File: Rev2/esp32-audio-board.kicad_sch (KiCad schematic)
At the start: 129 parts, among them IC1 LP2985A-33DBVR, J2 JST S2B, J21 IO32_PAD0, J3 USB_C_Receptacle_USB2.0_16P, J5 IO32_PAD1, J6 IO33_PAD0, J7 IO33_PAD1, J8 IO25_PAD0, J9 IO25_PAD1, Q1 SS8050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

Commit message: esp32-audio-board: add initial Rev2 schematic
Added an initial Rev2 schematic that contains all the main
components, except the connector to the sense board. This
can be decided later.
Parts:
- removed C39: 22uF/10%, Capacitor_SMD:C_0402_1005Metric_Pad0.74x0.62mm_HandSolder, symbol Device:C
- removed H4: MountingHole_Pad, MountingHole:MountingHole_2.2mm_M2_Pad_TopOnly, symbol Mechanical:MountingHole_Pad
- removed HP_G2: HP_GND2, solderpads:SolderPad_SMD_2x3mm, symbol Connector:Conn_01x01_Pin
- removed HP_L2: HP_LOUT2, solderpads:SolderPad_SMD_2x3mm, symbol Connector:Conn_01x01_Pin
- removed HP_R2: HP_ROUT2, solderpads:SolderPad_SMD_2x3mm, symbol Connector:Conn_01x01_Pin
- removed J2: JST S2B, Connector_JST:JST_PH_S2B-PH-K_1x02_P2.00mm_Horizontal, symbol Connector:Conn_01x02_Pin
- removed R32: 33R/1%, Resistor_SMD:R_0402_1005Metric_Pad0.72x0.64mm_HandSolder, symbol Device:R_US
- removed R37, R38: 100K/1%, Resistor_SMD:R_0402_1005Metric_Pad0.72x0.64mm_HandSolder, symbol Device:R_US
- removed TP1: T_SCL, TestPoint:TestPoint_Pad_D1.0mm, symbol Connector:TestPoint_Probe
- removed TP2: T_SDA, TestPoint:TestPoint_Pad_D1.0mm, symbol Connector:TestPoint_Probe
- added IC2: MAX17048G+T10, SON50P200X200X80-9N-D, symbol MAX17048G+T10:MAX17048G+T10
- added J1, J2: Conn_01x01_Pin, solderpads:SolderPad_SMD_2x2mm, symbol Connector:Conn_01x01_Pin
- C38: value 22uF/10% -> 0.1uF/10%
- R31: value 33R/1% -> 2K
- U2: DESCRIPTION USB to UART Bridge -> (none)
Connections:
- net ESP_IO35 is gone; now on net !ALRT: U1.7 (IO35)
- net +3V3: now also R31.1
- net ESP-IO0: no longer R24.1
- net GND: now also C38.2, IC2.1 (CTG), IC2.4 (GND), IC2.6 (QSTRT), IC2.9 (EP), J2.1 (Pin_1)
- net SCL: now also R23.2, IC2.7 (SCL); no longer R22.2
- net SDA: now also R22.2, IC2.8 (SDA); no longer R23.2
- net Serial-TX: now also R24.1
- net VBAT: now also C38.1, IC2.2 (CELL), IC2.3 (VDD), J1.1 (Pin_1)
- net !ALRT: now reaches R31.2
- net !ALRT: now also IC2.5 (~{ALRT})
- net ES8388_LOUT2: no longer names the net of U5.15 (LOUT2)
- net ES8388_LOUT2: no longer C38.1
- net ES8388_ROUT2: no longer names the net of U5.14 (ROUT2)
- no-connect marks 25 -> 27
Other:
- note added: "Fuel Gauge"
- note added: "I2C pull-ups"
- note added: "Place near the ESP32 module"
- note removed: "Battery Monitor"
- moved on the sheet: C19, C20, C21, C22, C23, C24, C25, C26, C27, C28, C29, C30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

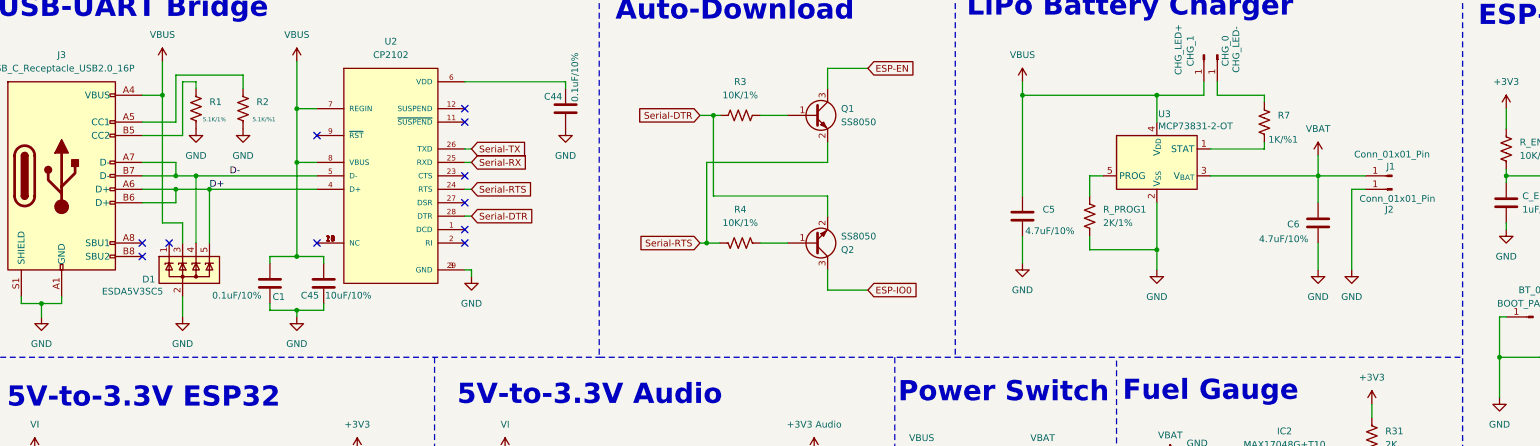
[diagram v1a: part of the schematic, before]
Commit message: esp32-audio-board: initial Rev2 PCB
Started working on the Rev2 PCB. Managed to get components
a lot closer and the PCB layout is more compact. The PCB
width got smaller by ~10mm.
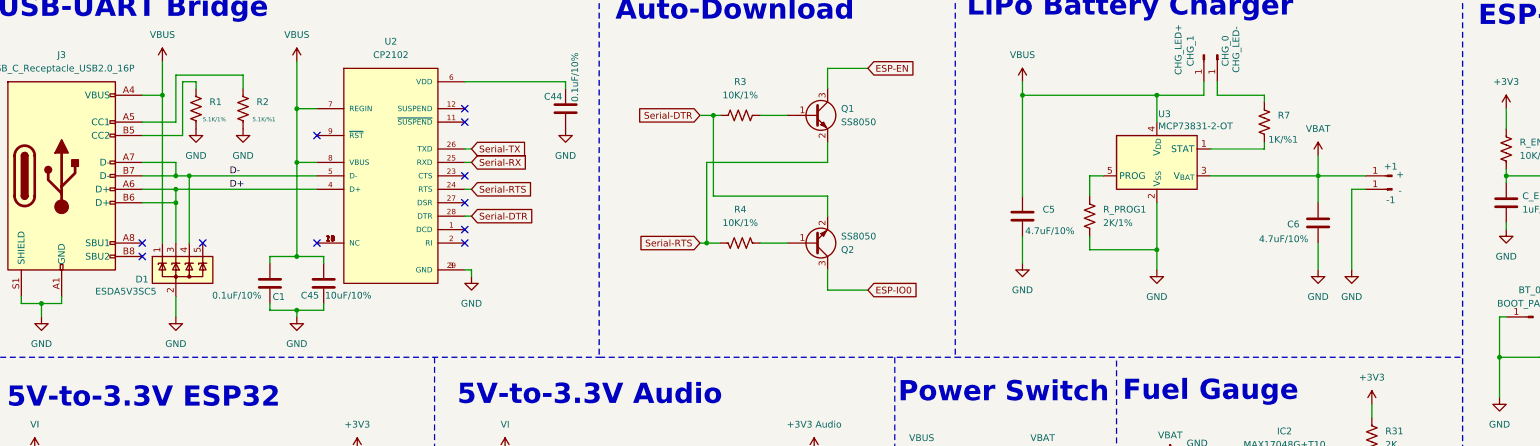
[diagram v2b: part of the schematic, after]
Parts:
- +1: renamed from J1; value Conn_01x01_Pin -> +
- -1: renamed from J2; value Conn_01x01_Pin -> -
- CHG_0, CHG_1, PWR_0, PWR_1: footprint solderpads:SolderPad_SMD_2x2mm -> solderpads:SolderPad_SMD_1x1mm
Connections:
- net D+: now also D1.3 (K); no longer D1.5 (K)
- net VBUS: now also D1.1 (K); no longer D1.3 (K)
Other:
- moved on the sheet: D1
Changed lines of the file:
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@@
 	)
 	(junction
-		(at 55.88 53.34)
+		(at 22.86 114.3)
 		(diameter 0)
 		(color 0 0 0 0)
 	)
 	(junction
-		(at 22.86 114.3)
+		(at 38.1 114.3)
 		(diameter 0)
 		(color 0 0 0 0)
 	)
 	(junction
-		(at 38.1 114.3)
+		(at 95.25 228.6)
 		(diameter 0)
 		(color 0 0 0 0)
 	)
 	(junction
-		(at 95.25 228.6)
+		(at 52.07 50.8)
 		(diameter 0)
 		(color 0 0 0 0)
@@
 	)
 	(junction
+		(at 49.53 55.88)
+		(diameter 0)
+		(color 0 0 0 0)
+	)
+	(junction
 		(at 24.13 74.93)
 		(diameter 0)
@@
 	)
 	(junction
-		(at 53.34 50.8)
-		(diameter 0)
-		(color 0 0 0 0)
-	)
-	(junction
 		(at 167.64 234.95)
 		(diameter 0)
@@
 	)
 	(no_connect
-		(at 48.26 63.5)
-	)
-	(no_connect
 		(at 370.84 91.44)
 	)
@@
 	)
 	(no_connect
+		(at 54.61 63.5)
+	)
+	(no_connect
 		(at 370.84 86.36)
 	)
@@
 	(wire
 		(pts
-			(xy 49.53 53.34) (xy 55.88 53.34)
+			(xy 49.53 53.34) (xy 76.2 53.34)
 		)
 		(stroke
@@
 	(wire
 		(pts
-			(xy 46.99 35.56) (xy 46.99 59.69)
+			(xy 46.99 35.56) (xy 46.99 63.5)
 		)
 		(stroke
@@
 	(wire
 		(pts
-			(xy 55.88 53.34) (xy 55.88 63.5)
-		)
-		(stroke
-			(width 0)
-			(type default)
-		)
-	)
-	(wire
-		(pts
 			(xy 368.3 189.23) (xy 368.3 193.04)
 		)
@@
 	(wire
 		(pts
-			(xy 50.8 73.66) (xy 50.8 77.47)
+			(xy 49.53 73.66) (xy 49.53 77.47)
 		)
 		(stroke
@@
 	(wire
 		(pts
-			(xy 53.34 50.8) (xy 76.2 50.8)
+			(xy 49.53 50.8) (xy 52.07 50.8)
 		)
 		(stroke
@@
 	(wire
 		(pts
-			(xy 50.8 59.69) (xy 50.8 63.5)
-		)
-		(stroke
-			(width 0)
-			(type default)
-		)
-	)
-	(wire
-		(pts
 			(xy 111.76 120.65) (xy 118.11 120.65)
 		)
@@
 	(wire
 		(pts
-			(xy 55.88 53.34) (xy 76.2 53.34)
-		)
-		(stroke
-			(width 0)
-			(type default)
-		)
-	)
-	(wire
-		(pts
 			(xy 41.91 238.76) (xy 44.45 238.76)
 		)
@@
 	(wire
 		(pts
-			(xy 53.34 50.8) (xy 53.34 63.5)
-		)
-		(stroke
-			(width 0)
-			(type default)
-		)
-	)
-	(wire
-		(pts
 			(xy 90.17 222.25) (xy 95.25 222.25)
 		)
@@
 	(wire
 		(pts
+			(xy 49.53 55.88) (xy 49.53 63.5)
+		)
+		(stroke
+			(width 0)
+			(type default)
+		)
+	)
+	(wire
+		(pts
 			(xy 121.92 245.11) (xy 123.19 245.11)
 		)
@@
 	(wire
 		(pts
+			(xy 52.07 50.8) (xy 52.07 63.5)
+		)
+		(stroke
+			(width 0)
+			(type default)
+		)
+	)
+	(wire
+		(pts
 			(xy 167.64 224.79) (xy 167.64 227.33)
 		)
@@
 	(wire
 		(pts
-			(xy 209.55 62.23) (xy 209.55 67.31)
+			(xy 52.07 50.8) (xy 76.2 50.8)
 		)
 		(stroke
@@
 	(wire
 		(pts
-			(xy 77.47 74.93) (xy 77.47 76.2)
+			(xy 209.55 62.23) (xy 209.55 67.31)
 		)
 		(stroke
@@
 	(wire
 		(pts
-			(xy 99.06 231.14) (xy 95.25 231.14)
+			(xy 77.47 74.93) (xy 77.47 76.2)
 		)
 		(stroke
@@
 	(wire
 		(pts
-			(xy 237.49 121.92) (xy 237.49 124.46)
+			(xy 99.06 231.14) (xy 95.25 231.14)
 		)
 		(stroke
@@
 	(wire
 		(pts
-			(xy 299.72 110.49) (xy 299.72 118.11)
+			(xy 237.49 121.92) (xy 237.49 124.46)
 		)
 		(stroke
@@
 	(wire
 		(pts
-			(xy 299.72 110.49) (xy 300.99 110.49)
+			(xy 299.72 110.49) (xy 299.72 118.11)
 		)
 		(stroke
@@
 	(wire
 		(pts
-			(xy 93.98 250.19) (xy 99.06 250.19)
+			(xy 299.72 110.49) (xy 300.99 110.49)
 		)
 		(stroke
@@
 	(wire
 		(pts
-			(xy 46.99 59.69) (xy 50.8 59.69)
+			(xy 93.98 250.19) (xy 99.06 250.19)
 		)
 		(stroke
@@
 	(wire
 		(pts
-			(xy 49.53 50.8) (xy 53.34 50.8)
-		)
-		(stroke
-			(width 0)
-			(type default)
-		)
-	)
-	(wire
-		(pts
 			(xy 321.31 110.49) (xy 321.31 114.3)
 		)
@@
 	)
 	(label "D+"
-		(at 55.88 53.34 0)
+		(at 59.69 53.34 0)
 		(effects
 			(font
@@
 			)
 		)
-		(property "Footprint" "solderpads:SolderPad_SMD_2x2mm"
+		(property "Footprint" "solderpads:SolderPad_SMD_1x1mm"
 			(at 246.38 27.94 0)
 			(hide yes)
@@
 			)
 		)
-		(property "Footprint" "solderpads:SolderPad_SMD_2x2mm"
+		(property "Footprint" "solderpads:SolderPad_SMD_1x1mm"
 			(at 90.17 129.54 0)
 			(hide yes)
@@
 	(symbol
 		(lib_id "power:GND")
-		(at 50.8 77.47 0)
+		(at 49.53 77.47 0)
 		(unit 1)
 		(body_style 1)
@@
 		(fields_autoplaced yes)
 		(property "Reference" "#PWR65"
-			(at 50.8 83.82 0)
+			(at 49.53 83.82 0)
 			(hide yes)
 			(show_name no)
@@
 		)
 		(property "Value" "GND"
-			(at 50.8 82.55 0)
+			(at 49.53 82.55 0)
 			(show_name no)
 			(do_not_autoplace no)
@@
 		)
 		(property "Footprint" ""
-			(at 50.8 77.47 0)
+			(at 49.53 77.47 0)
 			(hide yes)
 			(show_name no)
@@
 		)
 		(property "Datasheet" ""
-			(at 50.8 77.47 0)
+			(at 49.53 77.47 0)
 			(hide yes)
 			(show_name no)
@@
 		)
 		(property "Description" "Power symbol creates a global label with name \"GND\" , ground"
-			(at 50.8 77.47 0)
+			(at 49.53 77.47 0)
 			(hide yes)
 			(show_name no)
@@
 			)
 		)
-		(property "Footprint" "solderpads:SolderPad_SMD_2x2mm"
+		(property "Footprint" "solderpads:SolderPad_SMD_1x1mm"
 			(at 243.84 27.94 0)
 			(hide yes)
@@
 	(symbol
 		(lib_id "Power_Protection:ESDA5V3SC5")
-		(at 50.8 68.58 0)
+		(at 49.53 68.58 0)
 		(unit 1)
 		(body_style 1)
@@
 		(dnp no)
 		(property "Reference" "D1"
-			(at 43.18 70.358 0)
+			(at 41.91 70.358 0)
 			(show_name no)
 			(do_not_autoplace no)
@@
 		)
 		(property "Value" "ESDA5V3SC5"
-			(at 35.56 72.644 0)
+			(at 34.29 72.644 0)
 			(show_name no)
 			(do_not_autoplace no)
@@
 		)
 		(property "Footprint" "Package_TO_SOT_SMD:SOT-23-5_HandSoldering"
-			(at 58.42 69.85 0)
+			(at 57.15 69.85 0)
 			(hide yes)
 			(show_name no)
@@
 		)
 		(property "Datasheet" "https://www.st.com/resource/en/datasheet/esda5v3sc6.pdf"
-			(at 53.975 65.405 0)
+			(at 52.705 65.405 0)
 			(hide yes)
 			(show_name no)
@@
 		)
 		(property "Description" "Quad TVS Diode Array, 5.3V Standoff, 4 Channels, 400W, ±30kV, SOT-23-5"
-			(at 50.8 68.58 0)
+			(at 49.53 68.58 0)
 			(hide yes)
 			(show_name no)
@@
 		)
 		(property "Arrow Part Number" ""
-			(at 50.8 68.58 0)
+			(at 49.53 68.58 0)
 			(hide yes)
 			(show_name no)
@@
 		)
 		(property "Arrow Price/Stock" ""
-			(at 50.8 68.58 0)
+			(at 49.53 68.58 0)
 			(hide yes)
 			(show_name no)
@@
 			)
 		)
-		(property "Footprint" "solderpads:SolderPad_SMD_2x2mm"
+		(property "Footprint" "solderpads:SolderPad_SMD_1x1mm"
 			(at 90.17 127 0)
 			(hide yes)
@@
 		(in_pos_files yes)
 		(dnp no)
-		(property "Reference" "J1"
+		(property "Reference" "+1"
 			(at 279.146 49.022 0)
 			(show_name no)
@@
 			)
 		)
-		(property "Value" "Conn_01x01_Pin"
-			(at 279.4 46.736 0)
+		(property "Value" "+"
+			(at 280.924 50.546 0)
 			(show_name no)
 			(do_not_autoplace no)
@@
 			(project "esp32-audio-board"
 				(path "/eec632f9-36b4-4131-ab98-6e329881d10f"
-					(reference "J1")
+					(reference "+1")
 					(unit 1)
 				)
@@
 		(in_pos_files yes)
 		(dnp no)
-		(property "Reference" "J2"
-			(at 278.892 57.15 0)
+		(property "Reference" "-1"
+			(at 279.146 55.372 0)
 			(show_name no)
 			(do_not_autoplace no)
@@
 			)
 		)
-		(property "Value" "Conn_01x01_Pin"
-			(at 280.416 55.118 0)
+		(property "Value" "-"
+			(at 280.924 53.594 0)
 			(show_name no)
 			(do_not_autoplace no)
@@
 			(project "esp32-audio-board"
 				(path "/eec632f9-36b4-4131-ab98-6e329881d10f"
-					(reference "J2")
+					(reference "-1")
 					(unit 1)
 				)

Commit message: esp32-audio-board: Rev2 PCB done
Completed the work on the Rev2 PCB.
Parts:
- BT_0, BT_1, EN_0, EN_1, J21, J5, J6, J7, J8, J9: footprint solderpads:SolderPad_SMD_2x2mm -> solderpads:SolderPad_SMD_1x1mm
- C36, C37: value 22uF/10% -> 47uF/10%
- HP_G2: renamed from HP_G1; value HP_GND1 -> HP_GND2; footprint solderpads:SolderPad_SMD_2x3mm -> solderpads:SolderPad_SMD_1x2mm
- HP_L2: renamed from HP_L1; value HP_LOUT1 -> HP_LOUT2; footprint solderpads:SolderPad_SMD_2x3mm -> solderpads:SolderPad_SMD_1x2mm
- HP_R2: renamed from HP_R1; value HP_ROUT1 -> HP_ROUT2; footprint solderpads:SolderPad_SMD_2x3mm -> solderpads:SolderPad_SMD_1x2mm
- MI_L2: renamed from MI_L1; value MIC_LIN1 -> MIC_LIN2; footprint solderpads:SolderPad_SMD_2x3mm -> solderpads:SolderPad_SMD_1x2mm
- MI_LG2: renamed from MI_LG1; value MIC_LIN1_GND -> MIC_LIN2_GND; footprint solderpads:SolderPad_SMD_2x3mm -> solderpads:SolderPad_SMD_1x2mm
- MI_R2: renamed from MI_R1; value MIC_RIN1 -> MIC_RIN2; footprint solderpads:SolderPad_SMD_2x3mm -> solderpads:SolderPad_SMD_1x2mm
- MI_RG2: renamed from MI_RG1; value MIC_RIN1_GND -> MIC_RIN2_GND; footprint solderpads:SolderPad_SMD_2x3mm -> solderpads:SolderPad_SMD_1x2mm
- R29, R30: value 33R/1% -> 10R/1%
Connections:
- net !ALRT: no longer U1.7 (IO35)
- net BCK: now also U1.13 (IO14); no longer U1.16 (IO13)
- net DATA_IN: now also U1.10 (IO25); no longer U1.11 (IO26)
- net DATA_OUT: now also U1.12 (IO27); no longer U1.13 (IO14)
- net SCL: now also U1.9 (IO33); no longer U1.30 (IO18)
- net SDA: now also U1.8 (IO32); no longer U1.31 (IO19)
- net WS: now also U1.11 (IO26); no longer U1.12 (IO27)
- net ES8388_ROUT2: now reaches U5.14 (ROUT2)
- net ES8388_ROUT2: now also C37.1
- net ES8388_LOUT2: now reaches U5.15 (LOUT2)
- net ES8388_LOUT2: now also C36.1
- net ES8388_RIN2: now reaches U5.21 (RIN2)
- net ES8388_RIN2: now also C43.1
- net ES8388_LIN2: now reaches U5.22 (LIN2)
- net ES8388_LIN2: now also C40.1
- net ESP_IO23: now reaches U1.37 (IO23)
- net ESP_IO23: now also R16.1, R17.1
- net ESP_IO34: now reaches U1.6 (IO34)
- net ESP_IO34: now also R12.1, R13.1
- net ES8388_LIN1: no longer names the net of U5.24 (LIN1)
- net ES8388_LIN1: no longer C40.1
- net ES8388_LOUT1: no longer names the net of U5.12 (LOUT1)
- net ES8388_LOUT1: no longer C36.1
- net ES8388_RIN1: no longer names the net of U5.23 (RIN1)
- net ES8388_RIN1: no longer C43.1
- net ES8388_ROUT1: no longer names the net of U5.11 (ROUT1)
- net ES8388_ROUT1: no longer C37.1
- removed net ESP_IO25: R16.1, R17.1, U1.10 (IO25)
- removed net ESP_IO32: R12.1, R13.1, U1.8 (IO32)
- net ESP_IO33 renamed ESP_IO35
- net ESP_IO35: now also U1.7 (IO35); no longer U1.9 (IO33)
- no-connect marks 27 -> 28
